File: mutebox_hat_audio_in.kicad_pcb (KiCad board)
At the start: 2 copper layers, 65 x 56 mm, 52 parts, among them J1 GPIO, J2 PLR237/T10BK, J3 RCJ-042, J4 RCJ-042, U2 74LVC157, U3 PCM1862DBT, U5 DIR9001PW, Y3 XO32

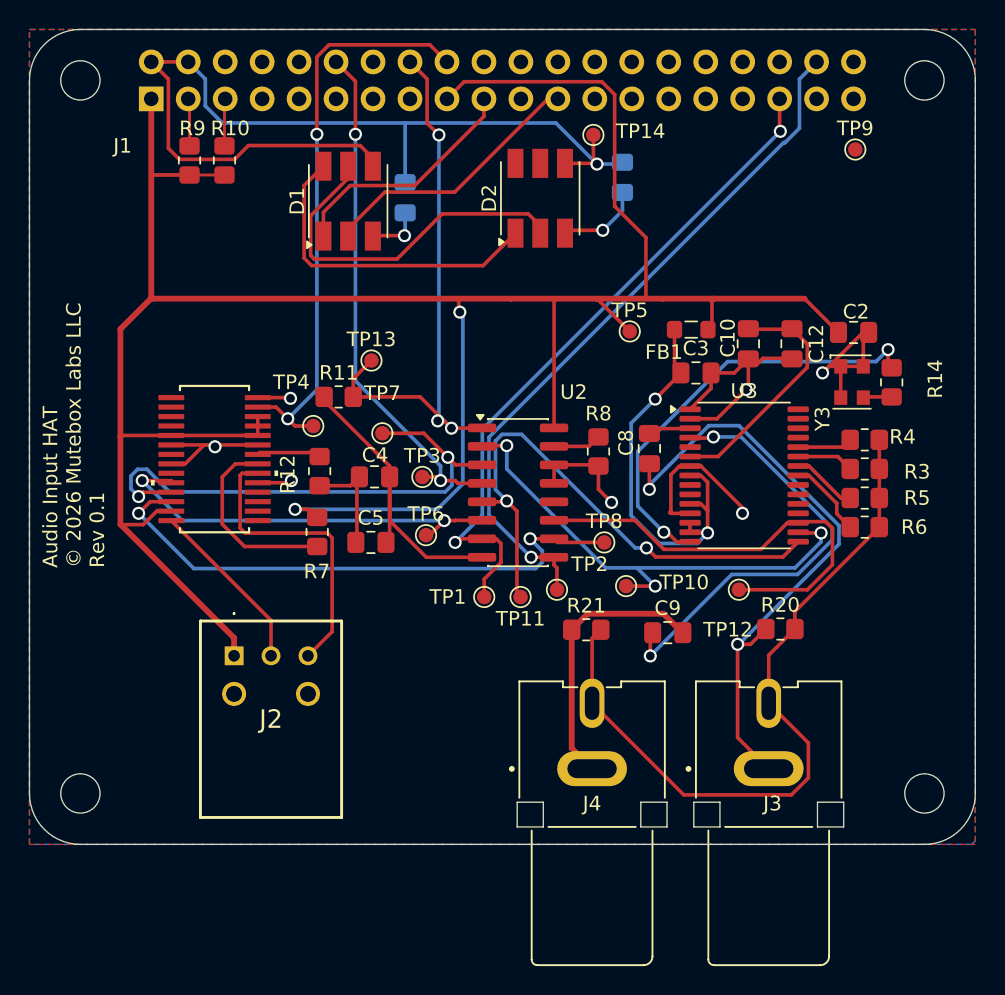
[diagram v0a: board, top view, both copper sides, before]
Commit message: Fixed 620 ohm resistor to 680.  Added parts for dotstart lights.  Added LCSC part numbers to components
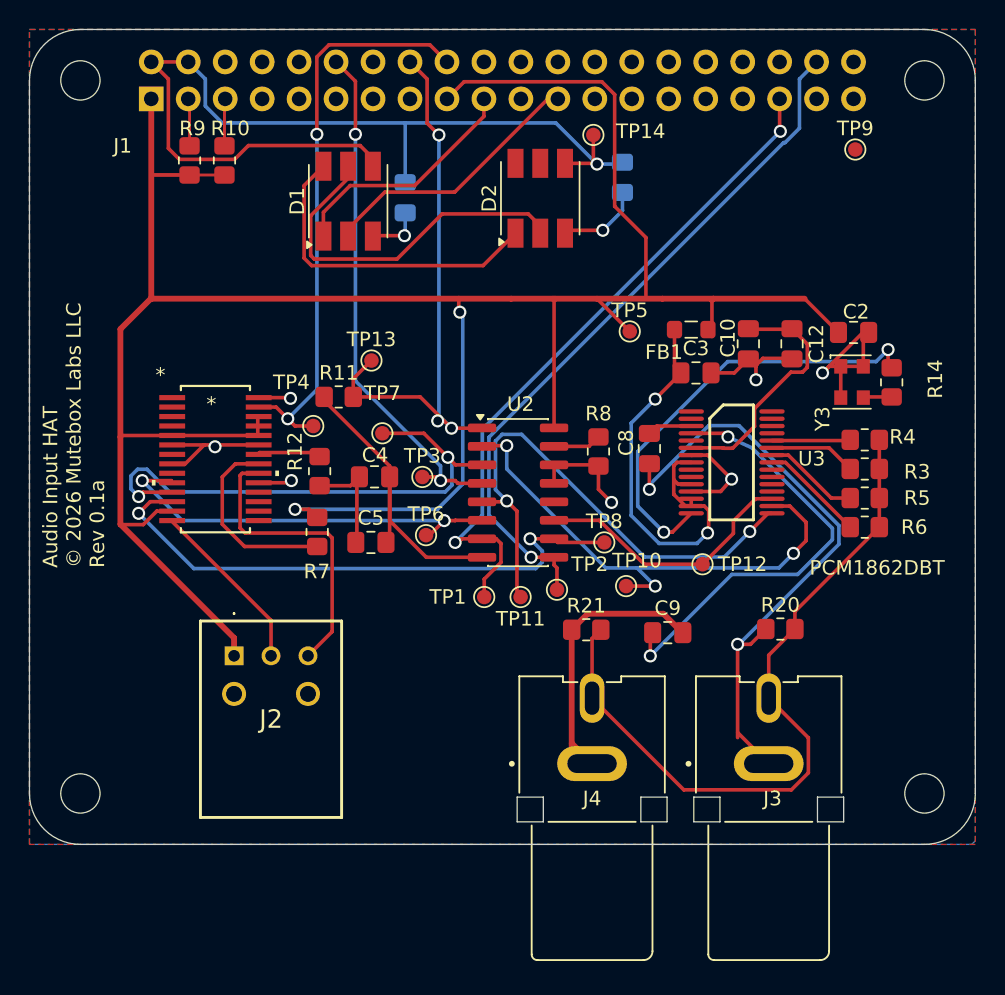
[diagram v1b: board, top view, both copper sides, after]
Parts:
- U3: footprint Package_SO:TSSOP-30_6.1x9.7mm_P0.65mm -> PCM1862DBT:DBT0030A_N
- moved TP12 3.05 mm to (146.2, 80.8)
- moved U3 1.25 mm to (148.2, 73.8)
- moved J3 0.35 mm to (150.8, 98.5)
- moved J4 0.35 mm to (138.7, 98.5)
- moved U5 0.06 mm to (112.8, 73.5)
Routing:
- net GND: track 155.1 -> 142.9 mm
- net ADC_SDOUT: track 30.6 -> 18.6 mm
- net MODE_FMT0: track 4.49 -> 6.60 mm
- net MODE_MS: track 3.93 -> 5.98 mm
- net MODE_FMT1: track 5.46 -> 7.22 mm
- net MD0: track 3.78 -> 5.40 mm
- net 3V3_A: track 28.2 -> 29.6 mm
- net ADC_LRCLK: track 37.7 -> 36.7 mm
- net ADC_BCLK: track 34.4 -> 35.3 mm
- net Net-(U3-VINL1/VIN1P): track 2.94 -> 3.62 mm
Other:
- board text added: "Audio Input HAT © 2026 Mutebox Labs LLC Rev 0.1a"
- board text removed: "Audio Input HAT © 2026 Mutebox Labs LLC Rev 0.1"

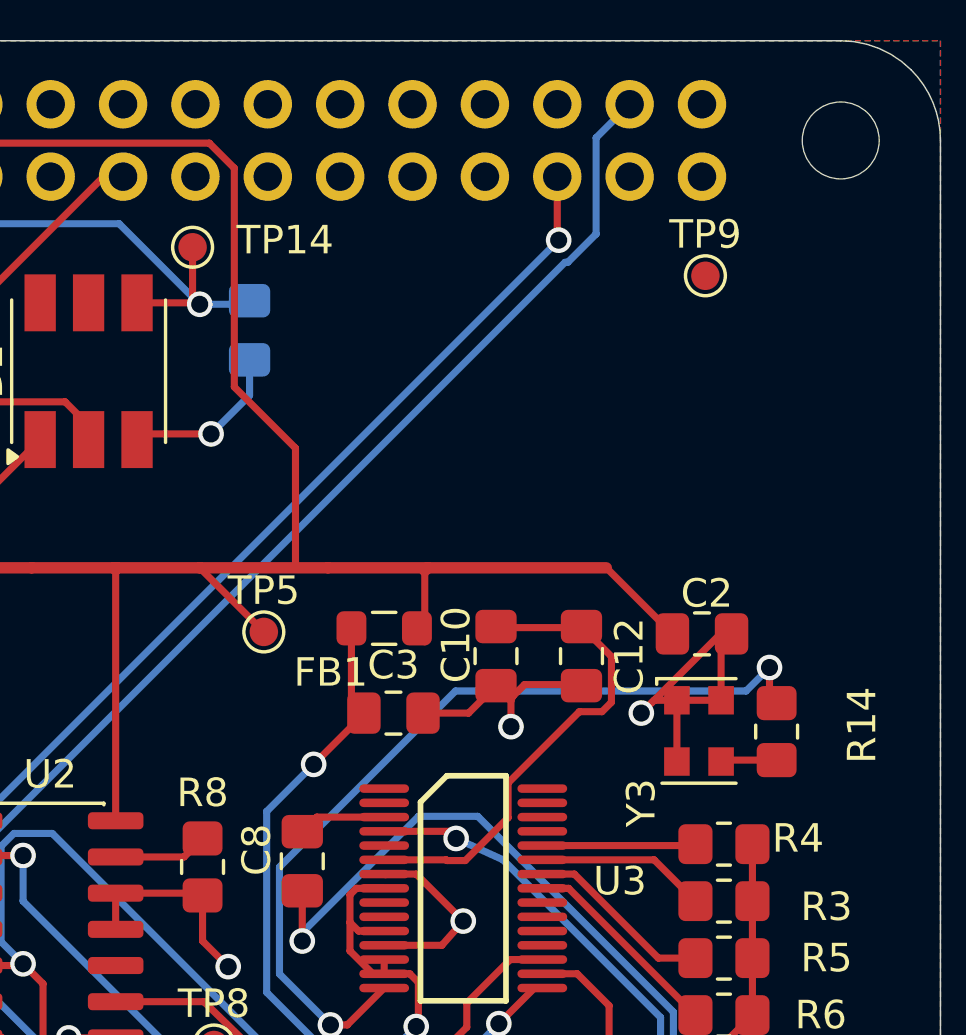
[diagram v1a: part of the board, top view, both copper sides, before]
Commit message: Added testpoint with large clip on footprint
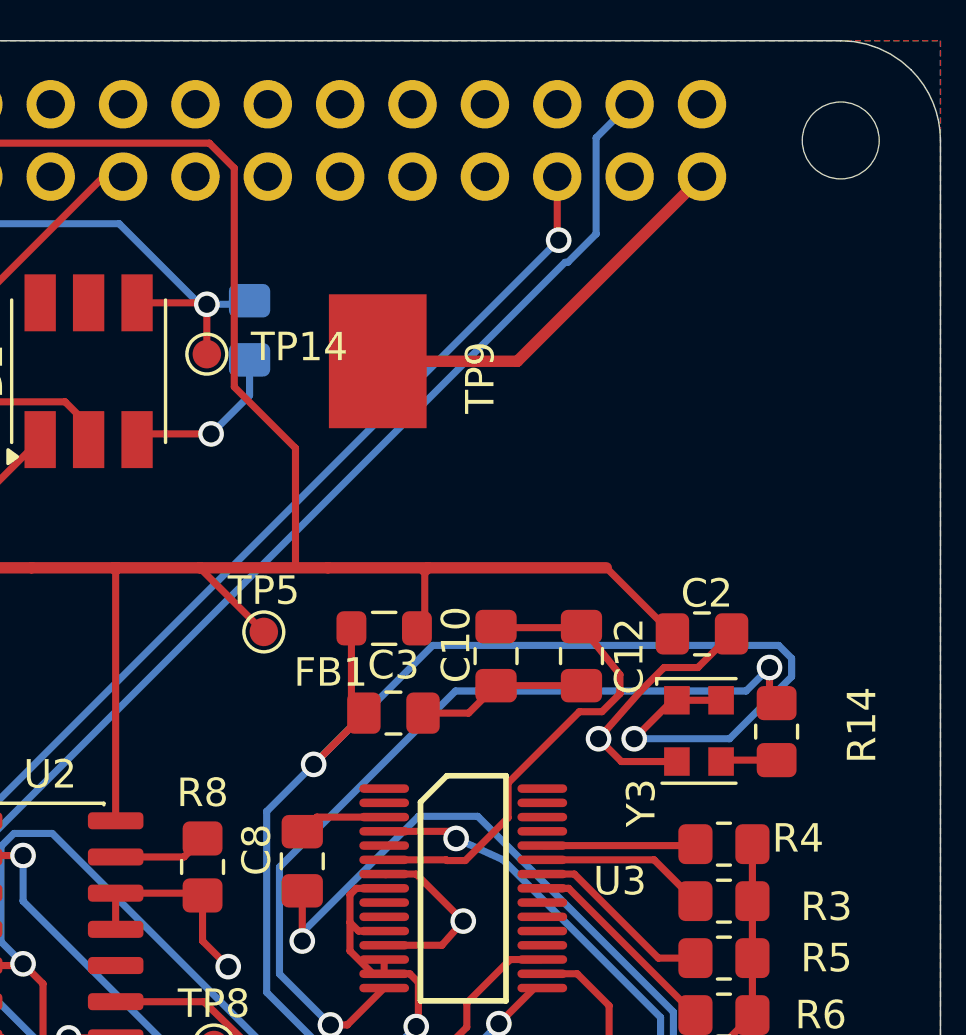
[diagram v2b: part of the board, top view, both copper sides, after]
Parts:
- TP9: value TP_GND -> 5016; footprint TestPoint:TestPoint_Pad_D1.0mm -> Connector:KEYSTONE_5016
- moved TP9 11.9 mm to (145.2, 55.2), turned to -90 degrees
- moved TP14 3.78 mm to (139.2, 55.0)
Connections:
- Y3 pad 1: GND -> 3V3_A
- Y3 pad 4: GND -> 3V3_A
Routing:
- net 3V3_A: track 29.6 -> 59.0 mm, vias 2 -> 3
- net GND: track 142.9 -> 153.4 mm, vias 9 -> 8

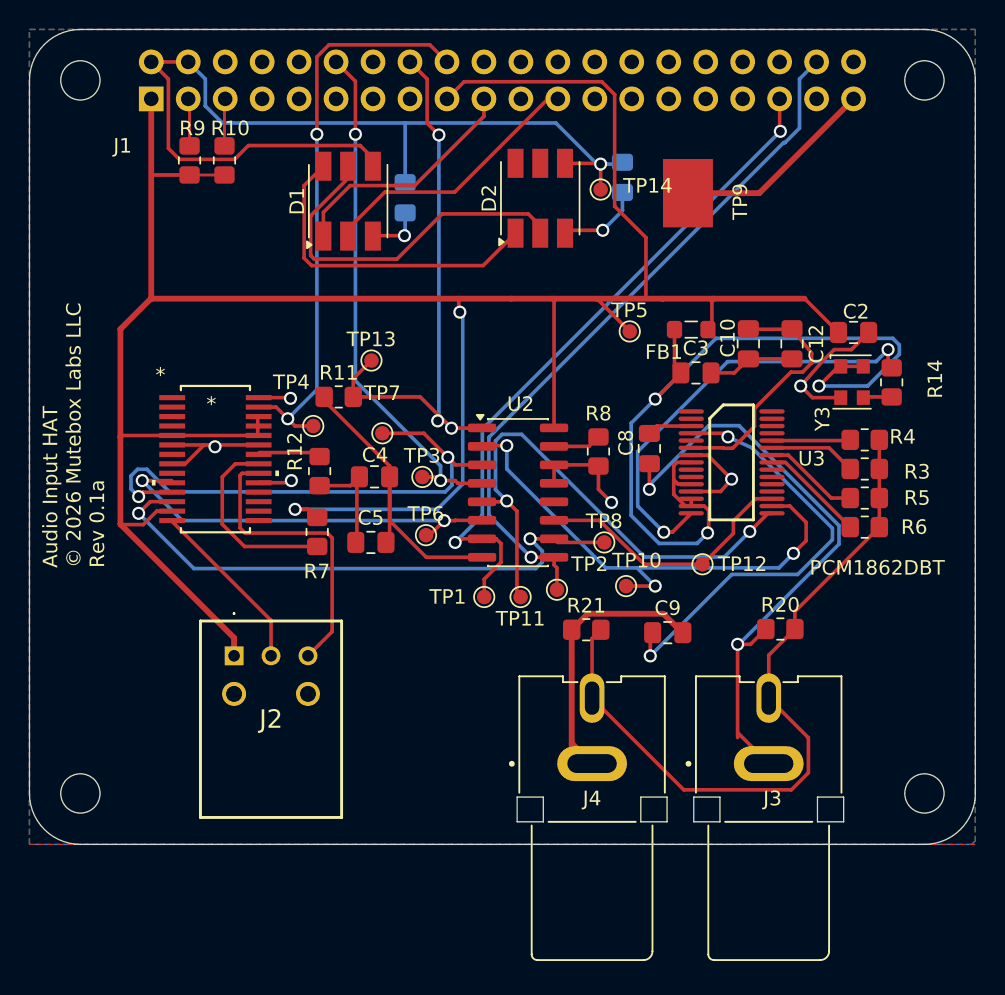
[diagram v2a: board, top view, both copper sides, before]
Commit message: Fixed dotstar positioning.  Minor changes to PCB
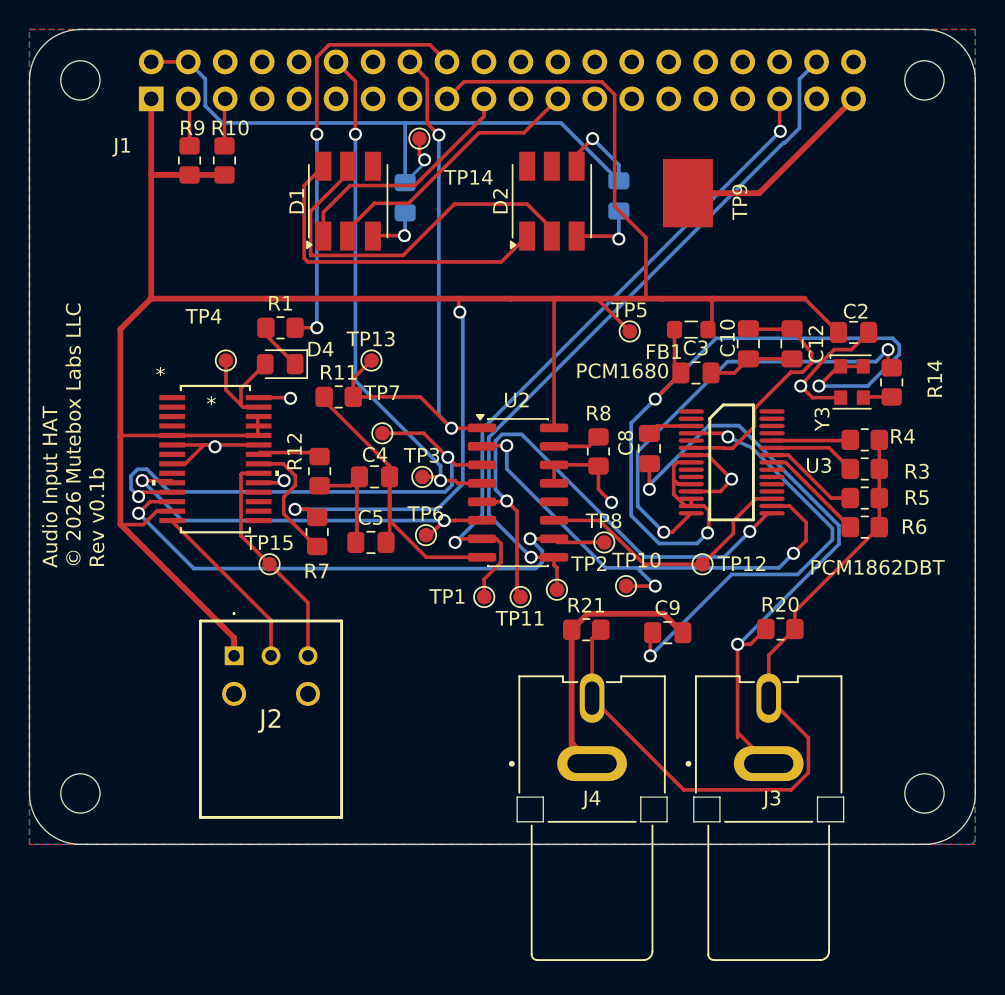
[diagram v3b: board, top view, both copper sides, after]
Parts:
- added D4: LED, LED_SMD:LED_0805_2012Metric_Pad1.15x1.40mm_HandSolder, F.Cu at (117.2, 67.0)
- added R1: 150, Resistor_SMD:R_0805_2012Metric_Pad1.20x1.40mm_HandSolder, F.Cu at (117.2, 64.5)
- added TP15: TP_RXIN, TestPoint:TestPoint_Pad_D1.0mm, F.Cu at (116.5, 80.8)
- moved TP14 12.9 mm to (126.8, 51.5)
- moved TP4 7.50 mm to (113.5, 66.8)
- moved C13 1.30 mm to (140.5, 55.4)
- moved D2 0.82 mm to (135.9, 55.8)
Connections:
- TP4 pad 1: TOSLINK_ERROR -> Net-(D4-A)
- U5 pad 27: TOSLINK_ERROR -> Net-(D4-A)
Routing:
- net +5V: track 66.1 -> 50.4 mm, vias 1 -> 2
- net TOSLINK_ERROR: track 39.8 -> 29.9 mm
- net Net-(D4-A): track 0.00 -> 7.74 mm
- net +3V3: track 173.8 -> 178.8 mm
- net Net-(J2-VOUT): track 20.3 -> 15.6 mm
- net Net-(U5-*RST): track 13.2 -> 9.04 mm
- net Net-(D4-K): track 0.00 -> 3.99 mm
- net /GPIO11/SPI0.SCLK: track 18.6 -> 20.6 mm
- net Net-(D1-CO): track 25.2 -> 26.7 mm
- net GND: track 153.4 -> 152.2 mm
- net Net-(D1-DO): track 22.5 -> 23.0 mm
- net GPIO23_OPT_LOCK: vias 3 -> 2
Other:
- board text added: "Audio Input HAT © 2026 Mutebox Labs LLC Rev v0.1b"
- board text removed: "Audio Input HAT © 2026 Mutebox Labs LLC Rev 0.1a"

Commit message: Added LED for OPT LOCK
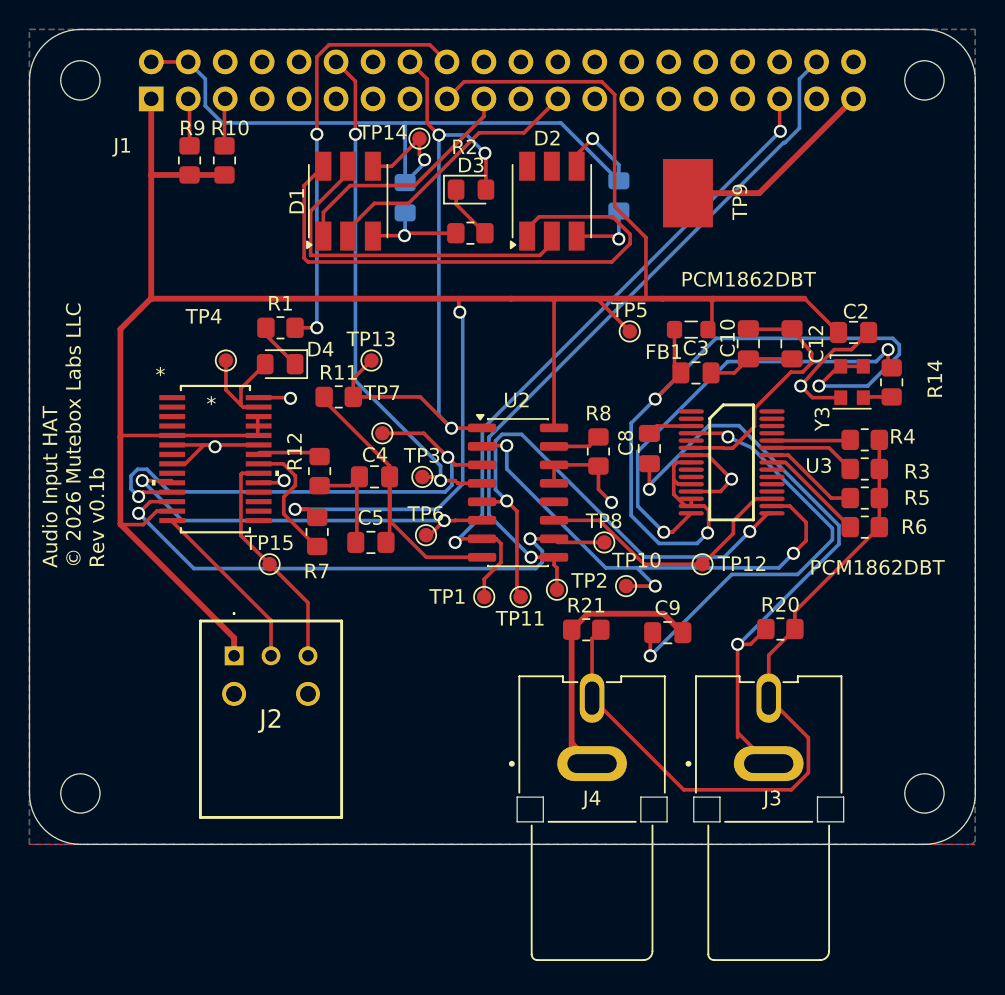
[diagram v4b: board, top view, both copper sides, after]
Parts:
- added D3: LED, LED_SMD:LED_0805_2012Metric_Pad1.15x1.40mm_HandSolder, F.Cu at (130.3, 55.0)
- added R2: 150, Resistor_SMD:R_0805_2012Metric_Pad1.20x1.40mm_HandSolder, F.Cu at (130.3, 58.0)
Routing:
- net Net-(D1-DO): track 23.0 -> 39.0 mm
- net GPIO23_OPT_LOCK: track 39.1 -> 45.3 mm, vias 2 -> 3
- net +5V: track 50.4 -> 54.4 mm
- net Net-(D3-K): track 0.00 -> 3.82 mm
- net GND: track 152.2 -> 155.8 mm
- net Net-(D1-CO): track 26.7 -> 24.6 mm

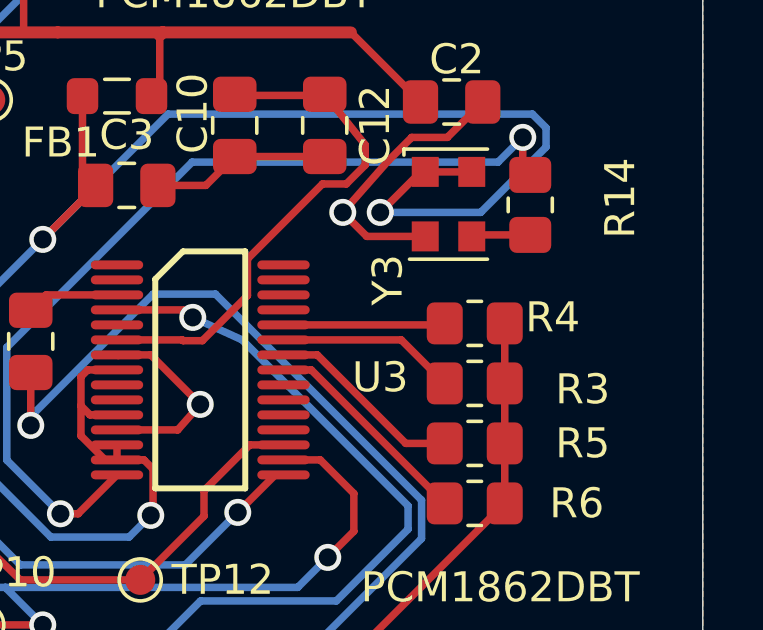
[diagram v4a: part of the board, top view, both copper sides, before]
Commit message: Fixed PCB for MODE_MS
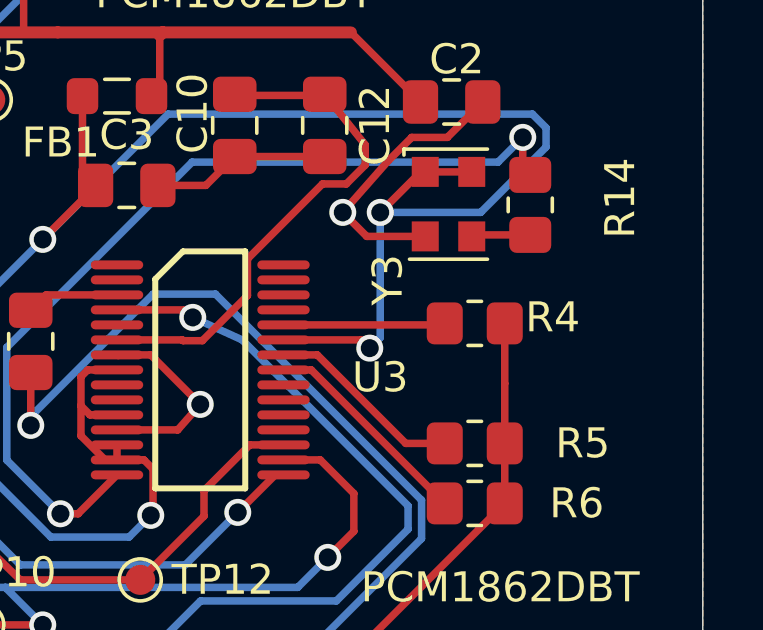
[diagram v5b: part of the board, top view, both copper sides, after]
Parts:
- removed R3: 10k, Resistor_SMD:R_0805_2012Metric_Pad1.20x1.40mm_HandSolder
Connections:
- U3 pad 25: MODE_MS -> 3V3_A
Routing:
- net 3V3_A: track 59.0 -> 66.6 mm, vias 3 -> 4
- net MODE_MS: track 5.98 -> 0.00 mm
